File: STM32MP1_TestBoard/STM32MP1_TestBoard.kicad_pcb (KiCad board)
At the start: 4 copper layers, 73.7 x 80 mm, 97 parts, among them J1 Conn_01x27, J12 Micro_SD_Card, J13 Micro_SD_Card, J14 USB_B_Micro, J15 USB_B, J2 Conn_01x27, J3 Conn_01x27, J4 Conn_01x27, J5 Conn_02x03_Odd_Even, J6 Conn_02x05_Odd_Even, J7 Conn_01x06, Q1 DMG2302U, SW2 SW_SPST, U1 STM32MP157xAB, U2 MT41K256M16TW-107, U3 SE8233X2, U4 TPS54202DDC

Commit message: update
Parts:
- removed J15: USB_B, Connector_USB:USB_B_Lumberg_2411_02_Horizontal
- removed JP2, JP3: Jumper_NC_Small, Jumper:SolderJumper-2_P1.3mm_Bridged_Pad1.0x1.5mm
- removed TP1, TP2, TP3: ~, TestPoint:TestPoint_Pad_D1.0mm
- added J8: USB_B_Micro, Connector_USB:USB_Micro-B_Molex-105017-0001, F.Cu at (160.8, 146.1)
- added R16: 0R, Resistor_SMD:R_0402_1005Metric_Pad0.72x0.64mm_HandSolder, F.Cu at (159.5, 141.7)
- added R17: 0R, Resistor_SMD:R_0402_1005Metric_Pad0.72x0.64mm_HandSolder, F.Cu at (162.1, 141.7)
- R11, R14, R2: moved to B.Cu
- moved C43 59.1 mm to (186.8, 109.8), turned to 270 degrees
- moved C36 58.6 mm to (189.0, 96.1), turned to 90 degrees
- moved C62 57.8 mm to (183.7, 96.0), turned to 90 degrees
- moved R2 54.8 mm to (180.8, 105.2)
- moved R15 54.5 mm to (177.2, 99.9), turned to 90 degrees
- moved C41 54.1 mm to (187.8, 109.8), turned to 270 degrees
- moved C65 53.3 mm to (184.8, 96.0), turned to 90 degrees
- moved C57 51.8 mm to (185.8, 96.0), turned to 90 degrees
- moved C52 51.5 mm to (187.9, 96.1), turned to 90 degrees
- moved R6 45.4 mm to (184.0, 109.5), turned to 270 degrees
- moved R52 45.1 mm to (186.9, 96.1), turned to 90 degrees
- moved C42 44.9 mm to (189.8, 109.8), turned to 270 degrees
- moved R14 44.0 mm to (184.6, 103.3), turned to 180 degrees
- moved C40 43.5 mm to (188.8, 109.8), turned to 270 degrees
- moved R11 36.1 mm to (183.5, 106.4), turned to 270 degrees
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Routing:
- net /DDR/DDR_DQ12: track 0.00 -> 34.4 mm, vias 0 -> 2
- net /DDR/DDR_DQ15: track 0.00 -> 34.1 mm, vias 0 -> 2
- net /DDR/DDR_DQ11: track 0.00 -> 31.8 mm, vias 0 -> 2
- net /DDR/DDR_DQ14: track 0.00 -> 31.4 mm, vias 0 -> 2
- net /DDR/DDR_DQS1_P: track 0.00 -> 28.2 mm, vias 0 -> 2
- net /DDR/DDR_DQS1_N: track 0.00 -> 27.8 mm, vias 0 -> 2
- net /DDR/DDR_DQS0_N: track 0.00 -> 27.3 mm
- net /DDR/DDR_DQS0_P: track 0.00 -> 27.0 mm
- net /DDR/DDR_DQ10: track 0.00 -> 25.4 mm, vias 0 -> 2
- net /DDR/DDR_DQ8: track 0.00 -> 24.9 mm, vias 0 -> 2
- net GNDS: track 115.4 -> 140.0 mm, vias 70 -> 97
- net /DDR/DDR_DQ6: track 0.00 -> 23.2 mm, vias 0 -> 2
- net /PSU/1.35V_VDDCORE: track 78.6 -> 99.9 mm, vias 41 -> 53
- net /DDR/DDR_CLK_P: track 0.00 -> 20.8 mm, vias 0 -> 1
- net /DDR/DDR_CKE: track 0.00 -> 20.7 mm, vias 0 -> 2
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
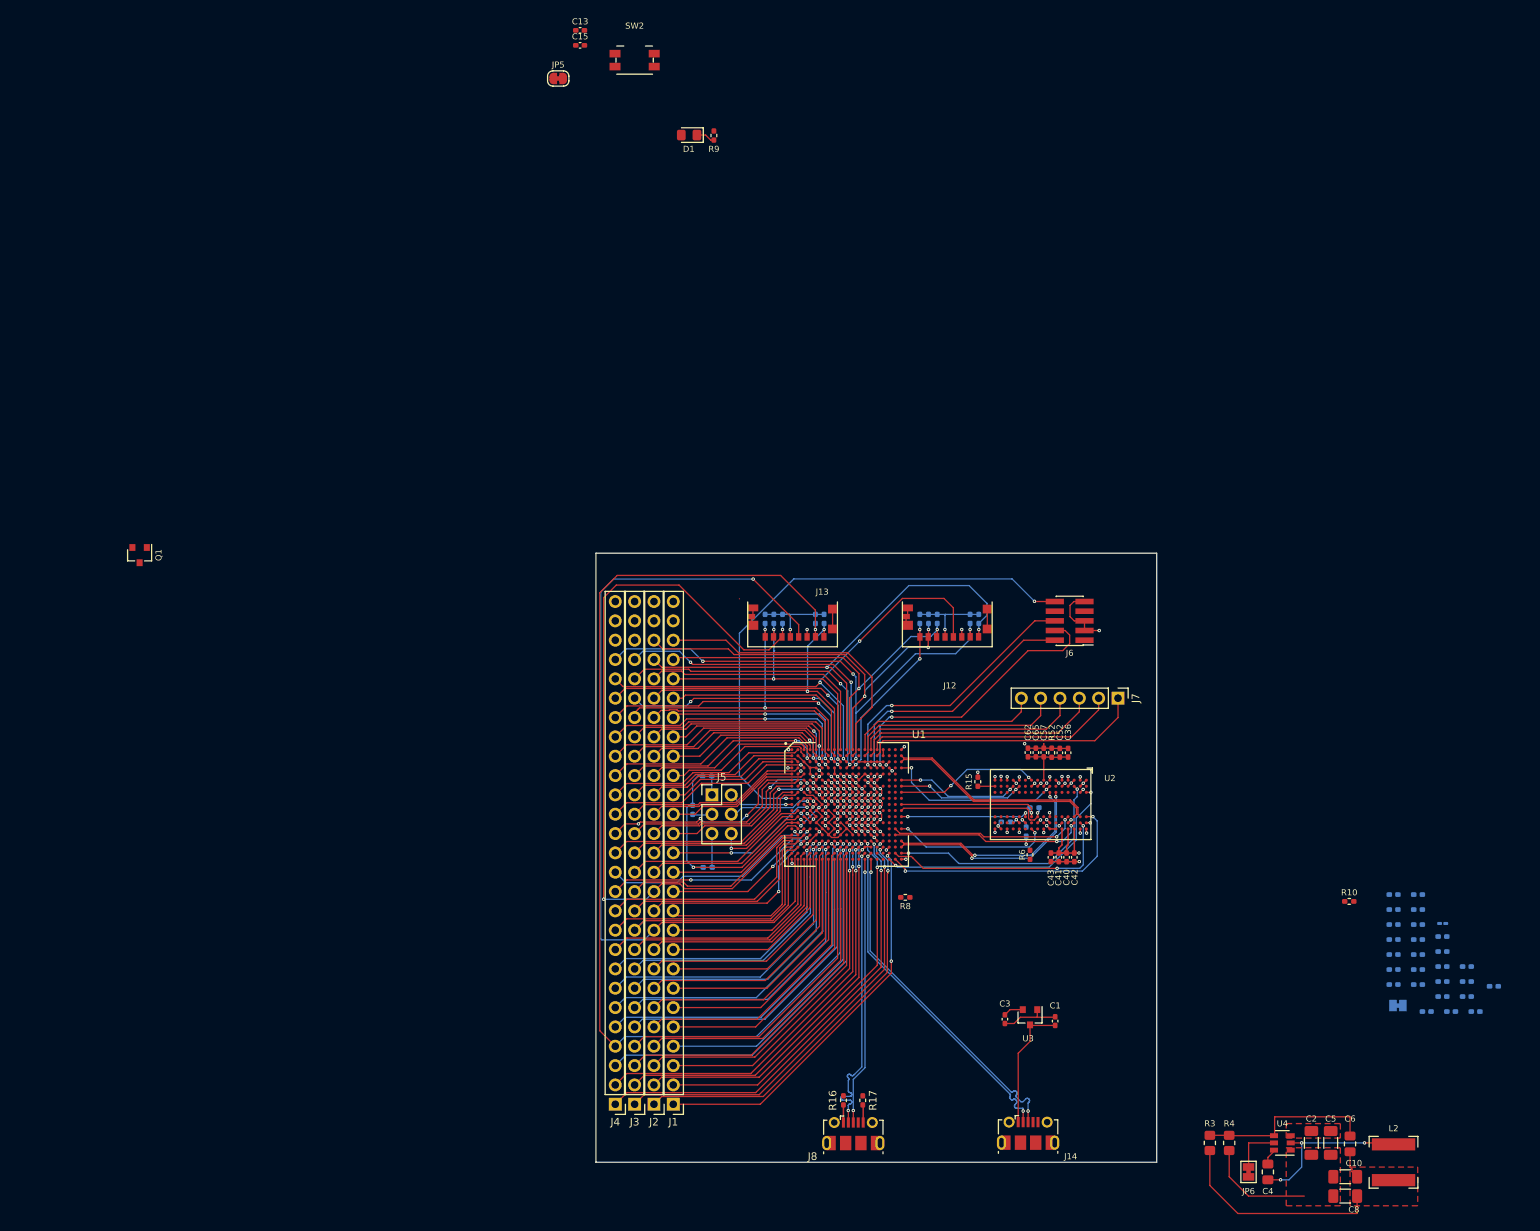
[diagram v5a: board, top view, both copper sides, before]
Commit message: added psu
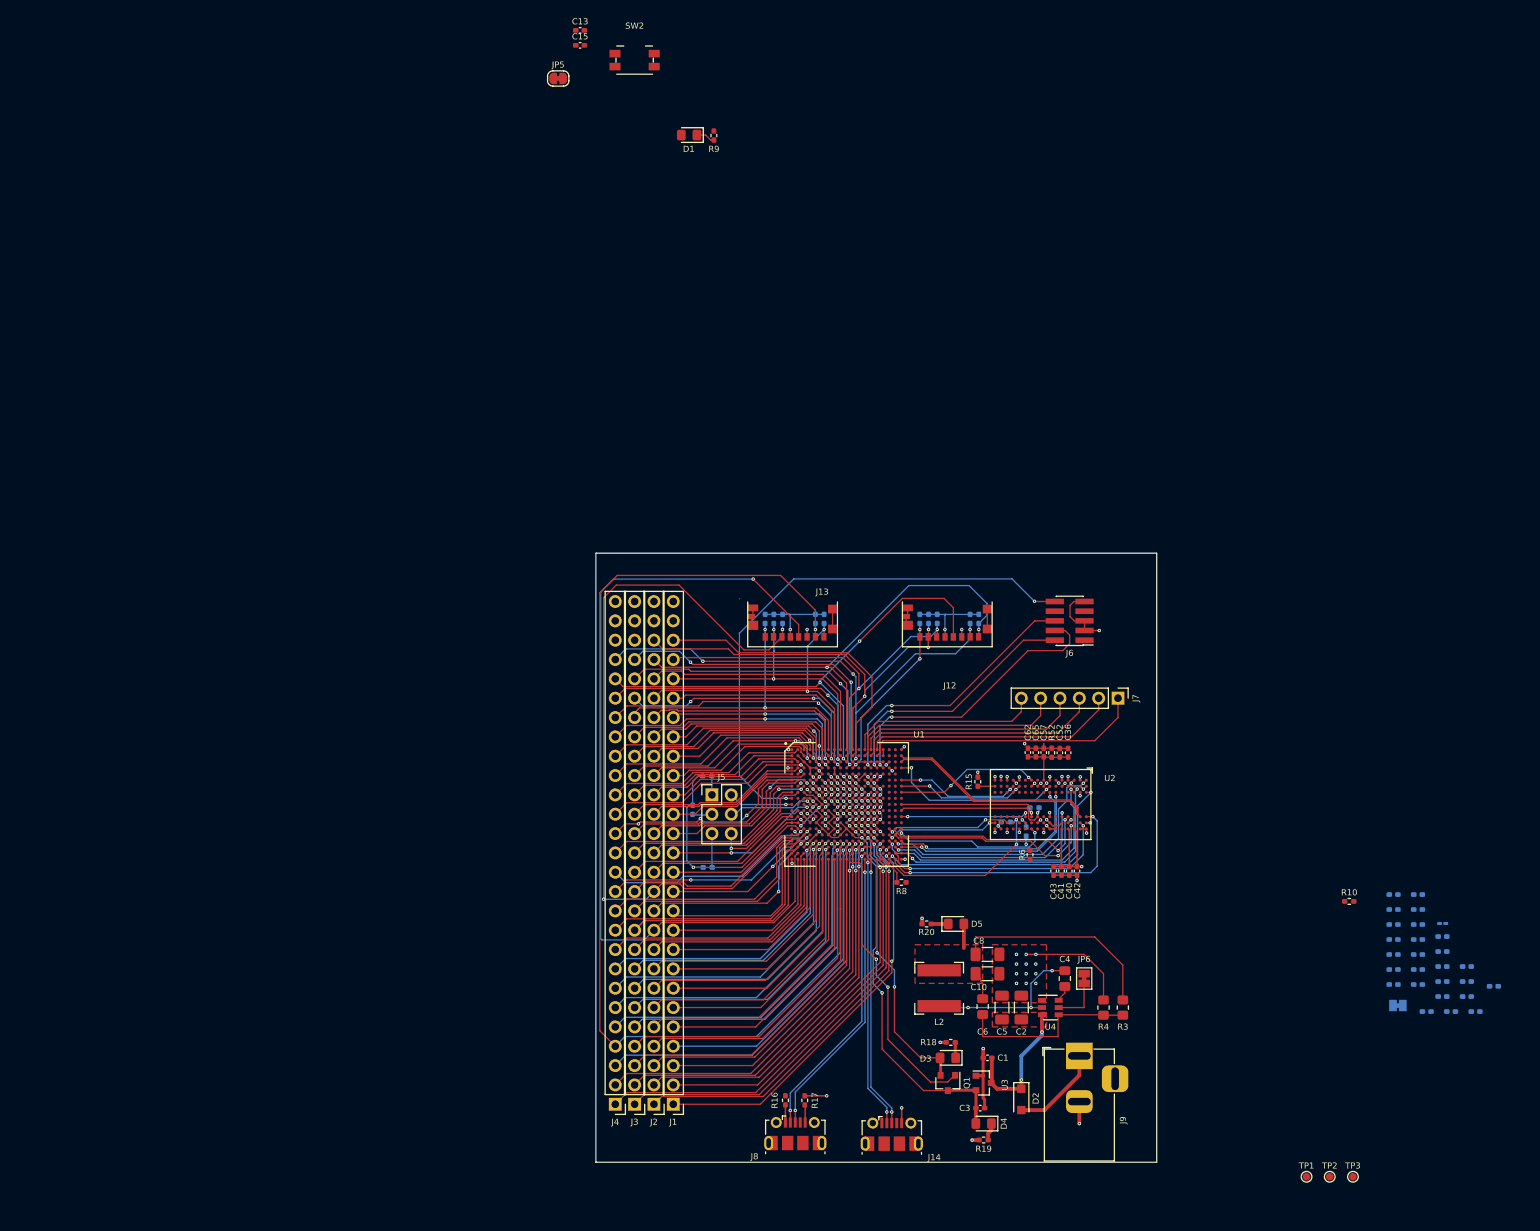
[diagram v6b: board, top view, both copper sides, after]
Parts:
- added D2: D_Schottky, Diode_SMD:D_SOD-123F, F.Cu at (182.9, 141.6)
- added D3: LED, LED_SMD:LED_0805_2012Metric_Pad1.15x1.40mm_HandSolder, F.Cu at (173.2, 136.1)
- added D4: LED, LED_SMD:LED_0805_2012Metric_Pad1.15x1.40mm_HandSolder, F.Cu at (177.9, 144.8)
- added D5: LED, LED_SMD:LED_0805_2012Metric_Pad1.15x1.40mm_HandSolder, F.Cu at (174.3, 118.6)
- added J9: Barrel_Jack, Connector_BarrelJack:BarrelJack_Horizontal, F.Cu at (190.5, 135.9)
- added R18: 2K2, Resistor_SMD:R_0402_1005Metric_Pad0.72x0.64mm_HandSolder, F.Cu at (173.6, 134.1)
- added R19: 2K2, Resistor_SMD:R_0402_1005Metric_Pad0.72x0.64mm_HandSolder, F.Cu at (177.9, 146.9)
- added R20: 2K2, Resistor_SMD:R_0402_1005Metric_Pad0.72x0.64mm_HandSolder, F.Cu at (170.4, 118.6)
- added TP1: ~, TestPoint:TestPoint_Pad_D1.0mm, F.Cu at (220.3, 151.8)
- added TP2: ~, TestPoint:TestPoint_Pad_D1.0mm, F.Cu at (223.4, 151.8)
- added TP3: ~, TestPoint:TestPoint_Pad_D1.0mm, F.Cu at (226.4, 151.8)
- moved Q1 126.8 mm to (173.2, 139.4)
- moved L2 63.9 mm to (172.1, 127.0), turned to 90 degrees
- moved C8 56.7 mm to (178.4, 122.6), turned to 0 degrees
- moved C10 54.0 mm to (178.4, 125.1), turned to 0 degrees
- moved C6 51.5 mm to (177.8, 129.4), turned to 90 degrees
- moved C5 46.7 mm to (180.3, 129.5), turned to 90 degrees
- moved C2 42.0 mm to (182.9, 129.5), turned to 90 degrees
- moved C4 36.8 mm to (188.6, 125.7), turned to 270 degrees
- moved U4 35.3 mm to (186.7, 129.5), turned to 0 degrees
- moved JP6 33.3 mm to (191.1, 125.7), turned to 270 degrees
- moved R4 24.3 mm to (193.7, 129.5), turned to 90 degrees
- moved R3 21.1 mm to (196.2, 129.5), turned to 270 degrees
- moved J14 17.9 mm to (165.9, 146.2)
- moved C3 12.1 mm to (177.5, 142.7), turned to 0 degrees
- moved U3 10.6 mm to (177.9, 139.4), turned to 0 degrees
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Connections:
- C1 pad 1: +5V -> Net-(C1-Pad1)
- C2 pad 1: +5V -> Net-(C1-Pad1)
- C5 pad 1: +5V -> Net-(C1-Pad1)
- U3 pad 3: +5V -> Net-(C1-Pad1)
- U4 pad 3: +5V -> Net-(C1-Pad1)
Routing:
- net /DebugInterface1/3.3V_VDD: track 80.6 -> 127.5 mm, vias 6 -> 8
- net /PSU/1V8_DETECT: track 0.00 -> 39.0 mm, vias 0 -> 2
- net /DDR/DDR_DQ9: track 0.00 -> 34.8 mm, vias 0 -> 2
- net /PSU/3V3_USB: track 0.00 -> 33.3 mm, vias 0 -> 2
- net /DDR/DDR_DQ13: track 0.00 -> 33.2 mm, vias 0 -> 2
- net /DDR/DDR_DQM1: track 0.00 -> 27.6 mm, vias 0 -> 2
- net /DDR/DDR_VREF: track 9.86 -> 33.2 mm, vias 1 -> 2
- net Net-(C1-Pad1): track 0.00 -> 18.6 mm, vias 0 -> 2
- net +5V: track 16.8 -> 0.00 mm
- net /DDR/DDR_A4: track 0.00 -> 16.5 mm, vias 0 -> 2
- net /DDR/DDR_A8: track 0.00 -> 14.9 mm, vias 0 -> 2
- net GNDS: track 140.0 -> 152.4 mm, vias 97 -> 114
- net Net-(D2-Pad2): track 0.00 -> 12.1 mm
- net /GPIO/USB_Conn/USB_D1_N: track 45.1 -> 35.8 mm
- net /GPIO/USB_Conn/USB_D1_P: track 45.2 -> 36.7 mm
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- added copper zone on F.Cu, net Net-(C1-Pad1)
- removed copper zone on F.Cu, net +5V

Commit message: update
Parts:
- moved C14 136.8 mm to (108.3, 121.7)
- moved C23 136.8 mm to (101.5, 123.0)
- moved C26 136.8 mm to (101.5, 121.1)
- moved C28 136.8 mm to (101.5, 115.1)
- moved C33 136.8 mm to (101.5, 119.1)
- moved C68 136.8 mm to (101.5, 117.1)
- moved R10 136.8 mm to (89.3, 110.5)
- moved C12 136.8 mm to (98.3, 113.6)
- moved C18 136.8 mm to (95.1, 119.5)
- moved C19 136.8 mm to (98.3, 121.4)
- moved C20 136.8 mm to (102.7, 125.0)
- moved C21 136.8 mm to (95.1, 117.5)
- moved C22 136.8 mm to (98.3, 119.5)
- moved C24 136.8 mm to (95.1, 115.5)
- moved C25 136.8 mm to (105.9, 125.0)
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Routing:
- net /DDR/DDR_DQ1: track 0.00 -> 32.4 mm, vias 0 -> 2
- net /DDR/DDR_DQ3: track 0.00 -> 31.6 mm, vias 0 -> 2
- net /DDR/DDR_DQM0: track 0.00 -> 28.6 mm, vias 0 -> 2
- net /DDR/DDR_DQ0: track 0.00 -> 28.6 mm, vias 0 -> 2
- net /DDR/DDR_DQ7: track 0.00 -> 28.1 mm, vias 0 -> 4
- net /DDR/DDR_DQ5: track 0.54 -> 28.1 mm, vias 1 -> 2
- net /DDR/DDR_DQ2: track 0.00 -> 22.7 mm, vias 0 -> 2
- net /DDR/DDR_RASN: track 0.00 -> 21.7 mm, vias 0 -> 2
- net /DDR/DDR_CASN: track 0.00 -> 21.5 mm, vias 0 -> 2
- net /DDR/DDR_DQ4: track 0.00 -> 21.3 mm, vias 0 -> 2
- net /DDR/DDR_CSN: track 0.00 -> 20.1 mm, vias 0 -> 2
- net /DDR/DDR_BA2: track 0.00 -> 18.9 mm, vias 0 -> 2
- net /DDR/DDR_WEN: track 0.00 -> 18.9 mm, vias 0 -> 2
- net /DDR/DDR_A5: track 0.00 -> 18.7 mm, vias 0 -> 2
- net /DDR/DDR_A12: track 0.00 -> 18.1 mm, vias 0 -> 2
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
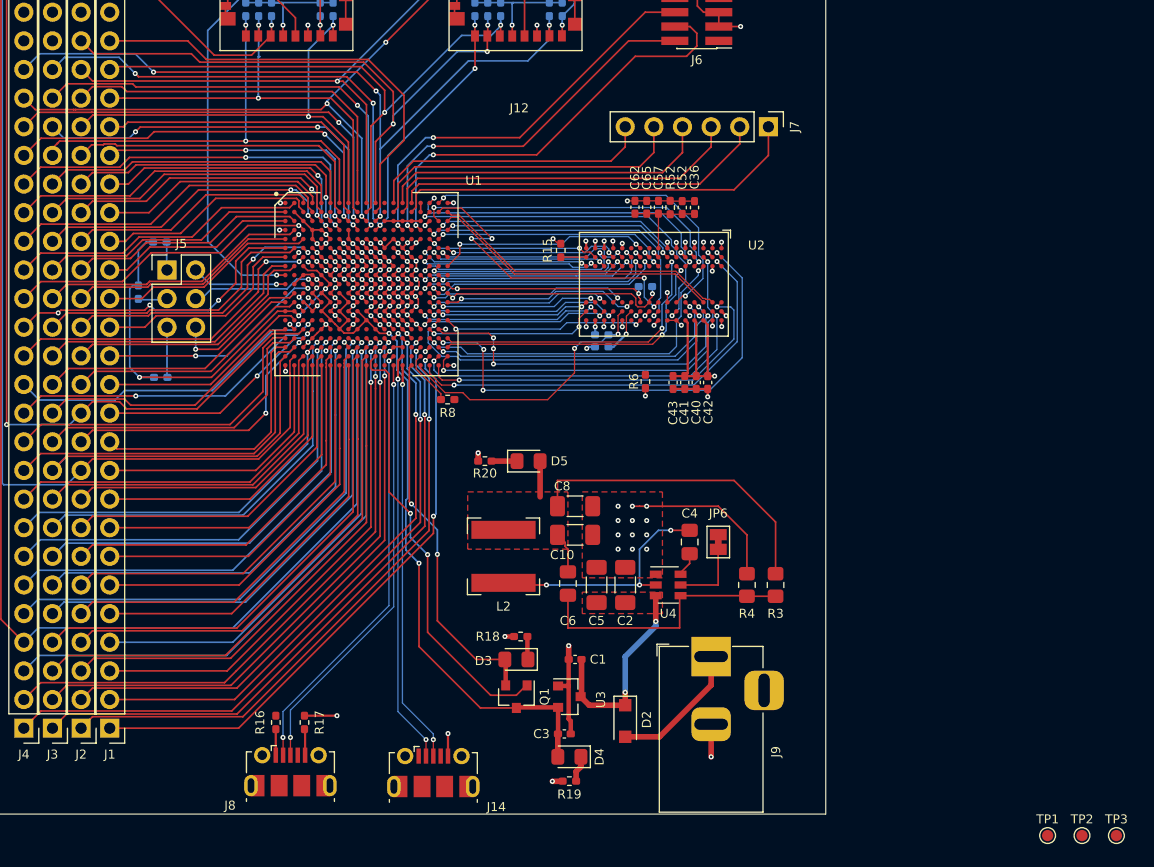
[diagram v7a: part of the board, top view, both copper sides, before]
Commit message: swapped DDR3 high/low strobe diff pairs
- corrected DRC errors
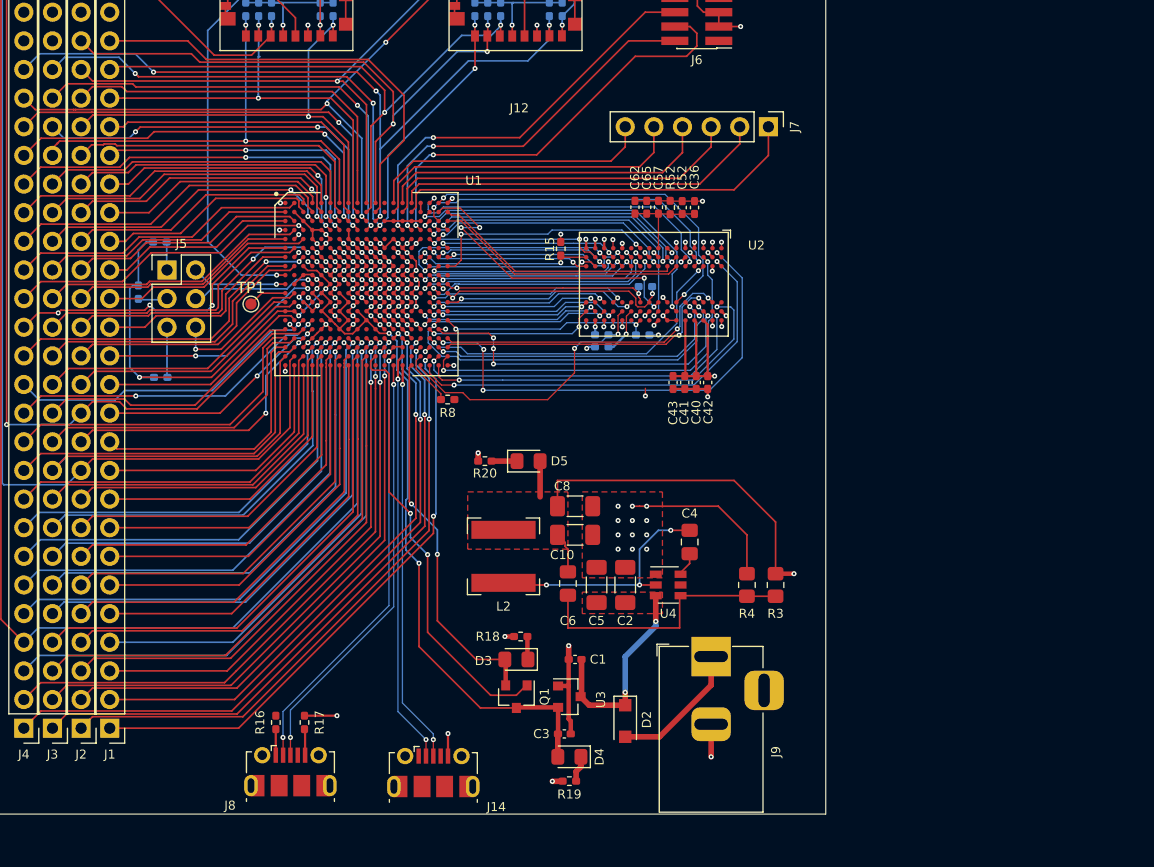
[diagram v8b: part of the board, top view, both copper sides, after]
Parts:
- removed JP6: Jumper_NC_Small, Jumper:SolderJumper-2_P1.3mm_Bridged_Pad1.0x1.5mm
- removed TP2, TP3: ~, TestPoint:TestPoint_Pad_D1.0mm
- R6: moved to B.Cu
- TP1: value ~ -> TestPoint
- moved TP1 84.9 mm to (149.7, 104.6)
- moved R6 4.13 mm to (184.4, 107.4), turned to 0 degrees
- moved R15 0.15 mm to (177.2, 99.7)
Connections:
- U1 pad L1: /PSU/PWR_ON -> Net-(TP1-Pad1)
- U1 pad N19: Net-(TP1-Pad1) -> Net-(U1-PadN19)
- U2 pad B7: /DDR/DDR_DQS0_N -> /DDR/DDR_DQS1_N
- U2 pad C7: /DDR/DDR_DQS0_P -> /DDR/DDR_DQS1_P
- U2 pad F3: /DDR/DDR_DQS1_P -> /DDR/DDR_DQS0_P
- U2 pad G3: /DDR/DDR_DQS1_N -> /DDR/DDR_DQS0_N
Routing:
- net Net-(R15-Pad1): track 2.28 -> 15.8 mm, vias 0 -> 2
- net Net-(U4-Pad5): track 6.50 -> 0.00 mm
- net /DDR/DDR_DQS0_N: track 26.8 -> 22.1 mm
- net Net-(TP1-Pad1): track 0.00 -> 3.45 mm
- net /DDR/DDR_DQS0_P: track 25.9 -> 22.5 mm
- net GNDS: track 151.8 -> 154.2 mm, vias 116 -> 117
- net /DDR/DDR_DQ2: track 22.7 -> 24.9 mm
- net /DDR/DDR_DQ6: track 21.1 -> 23.2 mm
- net /DDR/DDR_ODT: track 19.1 -> 20.4 mm
- net /DDR/DDR_DQ3: track 31.6 -> 30.3 mm
- net /PSU/1.35V_VDDCORE: track 110.3 -> 111.5 mm
- net /DDR/DDR_DQ9: track 30.9 -> 29.7 mm
- net /DDR/DDR_BA0: track 17.9 -> 16.9 mm
- net /DDR/DDR_CKE: track 17.9 -> 18.8 mm
- net /DDR/DDR_A13: track 15.4 -> 14.6 mm
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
